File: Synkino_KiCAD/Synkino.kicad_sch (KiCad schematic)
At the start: 161 parts, among them J1 Pwr, J10 EYE8_OUT, J11 EYE4_OUT, J12 2.5mm, J13 EYE5_OUT, J2 2.5mm, J3 3.5mm, J4 Micro_SD_Card_Det_Hirose_DM3AT, J5 EYE1_OUT, J6 EYE6_OUT, J7 EYE2_OUT, J8 EYE7_OUT, J9 EYE3_OUT, Q1 IRF7319, Q2 BC847 o. SS8050, Q3 IRLML2244 o. AO3401A, SW1 SW_Push, SW2 Rotary_Encoder_Switch, SW3 SW_Push, U1 MCP1702T-5002E/MB, U10 ATMEGA328P-AU, U11 QRE1113, U12 QRE1113, U13 QRE1113, U14 QRE1113, U15 QRE1113, U16 QRE1113, U17 24LC256, U18 QRE1113, U2 ATMEGA328P-AU, U3 74HC4050, U4 SPIOLED128x64, U5 AP7312-1833W6-7, U6 74HC14, U7 VS1053B, U8 MAX4741, U9 QRE1113, X1 FTDIconn, X2 ICSP, X3 FTDIconn, X4 ICSP, Y1 16Mhz, Y2 12.288MHz, Y3 16Mhz

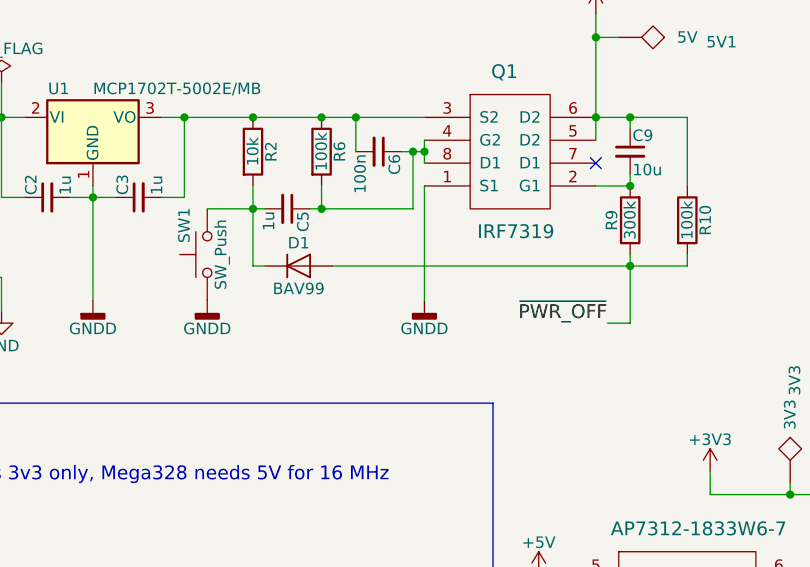
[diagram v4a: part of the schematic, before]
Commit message: Updating Reset Button, Footprints, adding 3v3 pane to Audio part
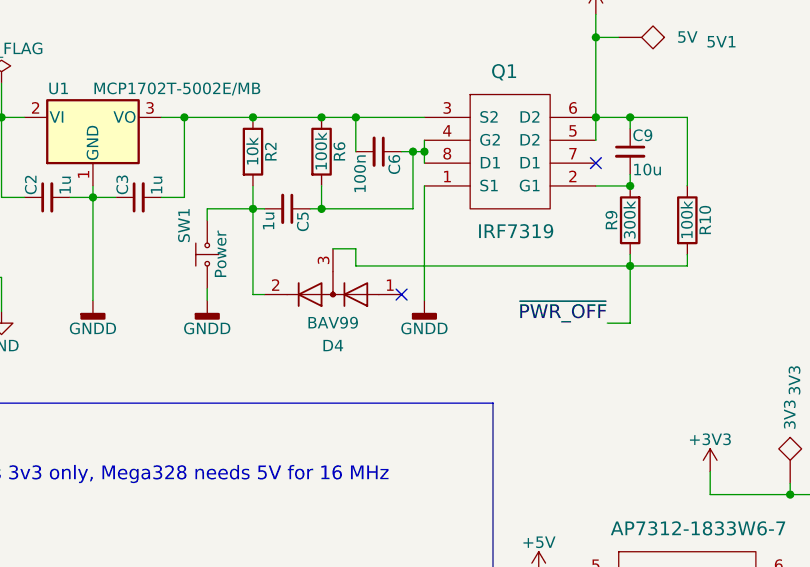
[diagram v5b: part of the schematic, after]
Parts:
- removed D1: BAV99, easyeda2kicad:SOT-23-3_L2.9-W1.3-P1.90-LS2.4-BR, symbol Synkino:D
- added D4: BAV99, Package_TO_SOT_SMD:SOT-23, symbol Diode:BAV99
- GND2, GNDA1: footprint TestPoint:TestPoint_Pad_2.0x2.0mm -> TestPoint:TestPoint_Pad_1.5x1.5mm
- J10, J11, J13, J5, J6, J7, J8, J9: footprint Connector_PinSocket_2.54mm:PinSocket_1x03_P2.54mm_Vertical -> Connector_PinHeader_2.54mm:PinHeader_1x03_P2.54mm_Vertical
- SW1: value SW_Push -> Power; symbol Synkino:SW_Push -> easyeda2kicad:B3F-5000_sm; LCSC Part (none) -> C93156
- X1, X3: footprint Connector_PinSocket_2.54mm:PinSocket_1x06_P2.54mm_Vertical -> Connector_PinHeader_2.54mm:PinHeader_1x06_P2.54mm_Vertical
- X2, X4: footprint Connector_PinSocket_2.54mm:PinSocket_2x03_P2.54mm_Vertical -> Connector_PinHeader_2.54mm:PinHeader_2x03_P2.54mm_Vertical
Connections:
- net GND: now also SW1.3, SW1.4; no longer SW1.1
- net ~{PWR_OFF}: now also D4.3 (K)
- net at C5.2, R2.2, SW1.2: now also SW1.1, D4.2 (A)
- no-connect marks 12 -> 13
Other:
- moved on the sheet: SW1
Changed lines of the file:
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@@
   (no_connect (at 242.57 54.61))
   (no_connect (at 292.1 132.08))
+  (no_connect (at 86.36 53.975))
   (no_connect (at 107.95 39.37))
   (no_connect (at 307.34 38.1))
@@
     (stroke (width 0) (type default))
   )
+  (wire (pts (xy 78.74 48.895) (xy 81.28 48.895))
+    (stroke (width 0) (type default))
+  )
   (wire (pts (xy 191.77 80.01) (xy 194.31 80.01))
     (stroke (width 0) (type default))
@@
     (stroke (width 0) (type default))
   )
+  (wire (pts (xy 69.85 53.975) (xy 71.12 53.975))
+    (stroke (width 0) (type default))
+  )
   (wire (pts (xy 245.11 92.71) (xy 252.73 92.71))
     (stroke (width 0) (type default))
@@
     (stroke (width 0) (type default))
   )
+  (wire (pts (xy 64.77 44.45) (xy 64.77 45.72))
+    (stroke (width 0) (type default))
+  )
   (wire (pts (xy 100.33 185.42) (xy 100.33 220.98))
     (stroke (width 0) (type default))
@@
     (stroke (width 0) (type default))
   )
-  (wire (pts (xy 69.85 44.45) (xy 69.85 50.8))
+  (wire (pts (xy 69.85 44.45) (xy 69.85 53.975))
     (stroke (width 0) (type default))
   )
@@
     (stroke (width 0) (type default))
   )
+  (wire (pts (xy 81.28 48.895) (xy 81.28 50.8))
+    (stroke (width 0) (type default))
+  )
   (wire (pts (xy 104.14 196.85) (xy 114.3 196.85))
     (stroke (width 0) (type default))
@@
     (stroke (width 0) (type default))
   )
-  (wire (pts (xy 78.74 50.8) (xy 111.76 50.8))
+  (wire (pts (xy 81.28 50.8) (xy 111.76 50.8))
     (stroke (width 0) (type default))
   )
@@
     (stroke (width 0) (type default))
   )
-  (wire (pts (xy 69.85 50.8) (xy 71.12 50.8))
-    (stroke (width 0) (type default))
-  )
   (wire (pts (xy 372.11 68.58) (xy 372.11 62.23))
     (stroke (width 0) (type default))
@@
     (stroke (width 0) (type default))
   )
+  (wire (pts (xy 64.77 53.34) (xy 64.77 54.61))
+    (stroke (width 0) (type default))
+  )
   (wire (pts (xy 170.18 111.76) (xy 170.18 114.3))
     (stroke (width 0) (type default))
@@
       (effects (font (size 1.524 1.524)))
     )
-    (property "Footprint" "Connector_PinSocket_2.54mm:PinSocket_2x03_P2.54mm_Vertical" (at 383.54 97.79 0)
+    (property "Footprint" "Connector_PinHeader_2.54mm:PinHeader_2x03_P2.54mm_Vertical" (at 383.54 97.79 0)
       (effects (font (size 1.524 1.524)) hide)
     )
@@
       (effects (font (size 1.524 1.524)))
     )
-    (property "Footprint" "Connector_PinSocket_2.54mm:PinSocket_1x06_P2.54mm_Vertical" (at 382.27 151.13 0)
+    (property "Footprint" "Connector_PinHeader_2.54mm:PinHeader_1x06_P2.54mm_Vertical" (at 382.27 151.13 0)
       (effects (font (size 1.524 1.524)) hide)
     )
@@
       (effects (font (size 1.524 1.524)))
     )
-    (property "Footprint" "Connector_PinSocket_2.54mm:PinSocket_2x03_P2.54mm_Vertical" (at 106.68 151.13 0)
+    (property "Footprint" "Connector_PinHeader_2.54mm:PinHeader_2x03_P2.54mm_Vertical" (at 106.68 151.13 0)
       (effects (font (size 1.524 1.524)) hide)
     )
@@
       (effects (font (size 1.524 1.524)))
     )
-    (property "Footprint" "Connector_PinSocket_2.54mm:PinSocket_1x06_P2.54mm_Vertical" (at 40.64 151.13 0)
+    (property "Footprint" "Connector_PinHeader_2.54mm:PinHeader_1x06_P2.54mm_Vertical" (at 40.64 151.13 0)
       (effects (font (size 1.524 1.524)) hide)
     )
@@
     )
   )
-  (symbol (lib_id "Synkino:D") (at 74.93 50.8 0) (unit 1)
-    (in_bom yes) (on_board yes) (dnp no)
-    (property "Reference" "D1" (at 74.93 48.26 0)
-      (effects (font (size 1.27 1.27)))
-    )
-    (property "Value" "BAV99" (at 74.93 53.34 0)
-      (effects (font (size 1.27 1.27)))
-    )
-    (property "Footprint" "easyeda2kicad:SOT-23-3_L2.9-W1.3-P1.90-LS2.4-BR" (at 74.93 50.8 0)
-      (effects (font (size 1.27 1.27)) hide)
-    )
-    (property "Datasheet" "" (at 74.93 50.8 0)
-      (effects (font (size 1.27 1.27)) hide)
-    )
-    (property "Inventory" "B" (at 74.93 50.8 0)
-      (effects (font (size 1.27 1.27)) hide)
-    )
-    (property "LCSC" "C2500" (at 74.93 50.8 0)
-      (effects (font (size 1.27 1.27)) hide)
-    )
-    (pin "1")
-    (pin "2")
-    (instances
-      (project "Synkino"
-        (path "/9d4924d9-a2ad-42f2-a951-8d7a9cc74761"
-          (reference "D1") (unit 1)
-        )
-      )
-    )
-  )
   (symbol (lib_id "Synkino:C_Small") (at 83.82 38.1 270) (unit 1)
     (in_bom yes) (on_board yes) (dnp no)
@@
     )
   )
-  (symbol (lib_id "Synkino:SW_Push") (at 64.77 49.53 90) (unit 1)
+  (symbol (lib_id "easyeda2kicad:B3F-5000_sm") (at 64.77 49.53 90) (unit 1)
     (in_bom yes) (on_board yes) (dnp no)
     (property "Reference" "SW1" (at 62.23 48.26 0)
       (effects (font (size 1.27 1.27)) (justify left))
     )
-    (property "Value" "SW_Push" (at 66.294 49.53 0)
+    (property "Value" "Power" (at 66.294 49.53 0)
       (effects (font (size 1.27 1.27)))
     )
-    (property "Footprint" "easyeda2kicad:KEY-TH_4P-L12.0-W12.0-P5.0-LS12.5-EH-small" (at 59.69 49.53 0)
+    (property "Footprint" "easyeda2kicad:KEY-TH_4P-L12.0-W12.0-P5.0-LS12.5-EH-small" (at 74.93 49.53 0)
       (effects (font (size 1.27 1.27)) hide)
     )
-    (property "Datasheet" "" (at 59.69 49.53 0)
+    (property "Datasheet" "https://lcsc.com/product-detail/Others_Omron-Electronics_B3F-5000_Omron-Electronics-B3F-5000_C93156.html" (at 77.47 49.53 0)
       (effects (font (size 1.27 1.27)) hide)
     )
@@
       (effects (font (size 1.27 1.27)) hide)
     )
+    (property "LCSC Part" "C93156" (at 80.01 49.53 0)
+      (effects (font (size 1.27 1.27)) hide)
+    )
     (pin "1")
     (pin "2")
+    (pin "4")
+    (pin "3")
     (instances
       (project "Synkino"
@@
       (effects (font (size 1.27 1.27)))
     )
-    (property "Footprint" "Connector_PinSocket_2.54mm:PinSocket_1x03_P2.54mm_Vertical" (at 339.09 181.61 0)
+    (property "Footprint" "Connector_PinHeader_2.54mm:PinHeader_1x03_P2.54mm_Vertical" (at 339.09 181.61 0)
       (effects (font (size 1.27 1.27)) hide)
     )
@@
       (effects (font (size 1.27 1.27)))
     )
-    (property "Footprint" "Connector_PinSocket_2.54mm:PinSocket_1x03_P2.54mm_Vertical" (at 309.88 181.61 0)
+    (property "Footprint" "Connector_PinHeader_2.54mm:PinHeader_1x03_P2.54mm_Vertical" (at 309.88 181.61 0)
       (effects (font (size 1.27 1.27)) hide)
     )
@@
       (effects (font (size 1.27 1.27)))
     )
-    (property "Footprint" "Connector_PinSocket_2.54mm:PinSocket_1x03_P2.54mm_Vertical" (at 400.05 181.61 0)
+    (property "Footprint" "Connector_PinHeader_2.54mm:PinHeader_1x03_P2.54mm_Vertical" (at 400.05 181.61 0)
       (effects (font (size 1.27 1.27)) hide)
     )
@@
       (effects (font (size 1.27 1.27)))
     )
-    (property "Footprint" "Connector_PinSocket_2.54mm:PinSocket_1x03_P2.54mm_Vertical" (at 370.84 181.61 0)
+    (property "Footprint" "Connector_PinHeader_2.54mm:PinHeader_1x03_P2.54mm_Vertical" (at 370.84 181.61 0)
       (effects (font (size 1.27 1.27)) hide)
     )
@@
       (effects (font (size 1.27 1.27)))
     )
-    (property "Footprint" "Connector_PinSocket_2.54mm:PinSocket_1x03_P2.54mm_Vertical" (at 309.88 220.98 0)
+    (property "Footprint" "Connector_PinHeader_2.54mm:PinHeader_1x03_P2.54mm_Vertical" (at 309.88 220.98 0)
       (effects (font (size 1.27 1.27)) hide)
     )
@@
       (effects (font (size 1.27 1.27)))
     )
-    (property "Footprint" "Connector_PinSocket_2.54mm:PinSocket_1x03_P2.54mm_Vertical" (at 370.84 220.98 0)
+    (property "Footprint" "Connector_PinHeader_2.54mm:PinHeader_1x03_P2.54mm_Vertical" (at 370.84 220.98 0)
       (effects (font (size 1.27 1.27)) hide)
     )
@@
       (effects (font (size 1.27 1.27)))
     )
-    (property "Footprint" "Connector_PinSocket_2.54mm:PinSocket_1x03_P2.54mm_Vertical" (at 339.09 220.98 0)
+    (property "Footprint" "Connector_PinHeader_2.54mm:PinHeader_1x03_P2.54mm_Vertical" (at 339.09 220.98 0)
       (effects (font (size 1.27 1.27)) hide)
     )
@@
       (effects (font (size 1.27 1.27)))
     )
-    (property "Footprint" "Connector_PinSocket_2.54mm:PinSocket_1x03_P2.54mm_Vertical" (at 400.05 220.98 0)
+    (property "Footprint" "Connector_PinHeader_2.54mm:PinHeader_1x03_P2.54mm_Vertical" (at 400.05 220.98 0)
       (effects (font (size 1.27 1.27)) hide)
     )
@@
       (effects (font (size 1.27 1.27)))
     )
-    (property "Footprint" "TestPoint:TestPoint_Pad_2.0x2.0mm" (at 209.55 121.92 0)
+    (property "Footprint" "TestPoint:TestPoint_Pad_1.5x1.5mm" (at 209.55 121.92 0)
       (effects (font (size 1.27 1.27)) hide)
     )
@@
       (effects (font (size 1.27 1.27)))
     )
-    (property "Footprint" "TestPoint:TestPoint_Pad_2.0x2.0mm" (at 204.47 121.92 0)
+    (property "Footprint" "TestPoint:TestPoint_Pad_1.5x1.5mm" (at 204.47 121.92 0)
       (effects (font (size 1.27 1.27)) hide)
     )
@@
         )
       )
+    )
+  )
+  (symbol (lib_id "Diode:BAV99") (at 78.74 53.975 180) (unit 1)
+    (in_bom yes) (on_board yes) (dnp no)
+    (property "Reference" "D4" (at 78.74 59.69 0)
+      (effects (font (size 1.27 1.27)))
+    )
+    (property "Value" "BAV99" (at 78.74 57.15 0)
+      (effects (font (size 1.27 1.27)))
+    )
+    (property "Footprint" "Package_TO_SOT_SMD:SOT-23" (at 78.74 41.275 0)
+      (effects (font (size 1.27 1.27)) hide)
+    )
+    (property "Datasheet" "https://assets.nexperia.com/documents/data-sheet/BAV99_SER.pdf" (at 78.74 53.975 0)
+      (effects (font (size 1.27 1.27)) hide)
+    )
+    (property "Inventory" "B" (at 78.74 53.975 0)
+      (effects (font (size 1.27 1.27)) hide)
+    )
+    (property "LCSC" "C2500" (at 78.74 53.975 0)
+      (effects (font (size 1.27 1.27)) hide)
+    )
+    (pin "2")
+    (pin "3")
+    (pin "1")
+    (instances
+      (project "Synkino"
+        (path "/9d4924d9-a2ad-42f2-a951-8d7a9cc74761"
+          (reference "D4") (unit 1)
+        )
+      )

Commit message: DRC mostly happy now
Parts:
- 3V3, 5V1: footprint TestPoint:TestPoint_Pad_1.5x1.5mm -> TestPoint:TestPoint_THTPad_1.5x1.5mm_Drill0.7mm
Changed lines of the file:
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@@
       (effects (font (size 1.27 1.27)))
     )
-    (property "Footprint" "TestPoint:TestPoint_Pad_1.5x1.5mm" (at 110.49 25.4 0)
+    (property "Footprint" "TestPoint:TestPoint_THTPad_1.5x1.5mm_Drill0.7mm" (at 110.49 25.4 0)
       (effects (font (size 1.27 1.27)) hide)
     )
@@
       (effects (font (size 1.27 1.27)))
     )
-    (property "Footprint" "TestPoint:TestPoint_Pad_1.5x1.5mm" (at 129.54 74.93 0)
+    (property "Footprint" "TestPoint:TestPoint_THTPad_1.5x1.5mm_Drill0.7mm" (at 129.54 74.93 0)
       (effects (font (size 1.27 1.27)) hide)
     )

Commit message: Updated legacy footprint associations
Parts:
- BZ1: footprint lib_fp:AAC801J-13 -> Peacemans_Footprints:AAC801J-13
- J12, J2: footprint Synkino:SJ1-2503 -> Peacemans_Footprints:SJ1-2503
- J3: footprint lib_fp:SJ1-352XNG -> Peacemans_Footprints:SJ1-352XNG
- J4: footprint lib_fp:HRS_DM3AT-SF-PEJM5 -> Peacemans_Footprints:HRS_DM3AT-SF-PEJM5
- SW2: footprint lib_fp:SW_PEC11 -> Peacemans_Footprints:SW_PEC11
- U11, U12, U13, U14, U15, U16, U18, U9: footprint lib_fp:QRE1113GR -> Peacemans_Footprints:QRE1113GR
- U4: footprint lib_fp:SPIOLED -> Peacemans_Footprints:SPIOLED
- U5: footprint lib_fp:AP7312 -> Peacemans_Footprints:AP7312
- Y1, Y2, Y3: footprint lib_fp:CRYSTAL_7A -> Peacemans_Footprints:CRYSTAL_7A
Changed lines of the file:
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@@
       (effects (font (size 1.524 1.524)))
     )
-    (property "Footprint" "lib_fp:AP7312" (at 114.3 88.9 0)
+    (property "Footprint" "Peacemans_Footprints:AP7312" (at 114.3 88.9 0)
       (effects (font (size 1.524 1.524)) hide)
     )
@@
       (effects (font (size 1.27 1.27)))
     )
-    (property "Footprint" "lib_fp:CRYSTAL_7A" (at 173.99 105.41 0)
+    (property "Footprint" "Peacemans_Footprints:CRYSTAL_7A" (at 173.99 105.41 0)
       (effects (font (size 1.27 1.27)) hide)
     )
@@
       (effects (font (size 1.27 1.27)) (justify right))
     )
-    (property "Footprint" "lib_fp:HRS_DM3AT-SF-PEJM5" (at 382.27 30.48 0)
+    (property "Footprint" "Peacemans_Footprints:HRS_DM3AT-SF-PEJM5" (at 382.27 30.48 0)
       (effects (font (size 1.27 1.27)) hide)
     )
@@
       (effects (font (size 1.524 1.524)))
     )
-    (property "Footprint" "lib_fp:SPIOLED" (at 118.11 276.86 0)
+    (property "Footprint" "Peacemans_Footprints:SPIOLED" (at 118.11 276.86 0)
       (effects (font (size 1.524 1.524)) hide)
     )
@@
       (effects (font (size 1.27 1.27)))
     )
-    (property "Footprint" "lib_fp:CRYSTAL_7A" (at 80.01 190.5 0)
+    (property "Footprint" "Peacemans_Footprints:CRYSTAL_7A" (at 80.01 190.5 0)
       (effects (font (size 1.27 1.27)) hide)
     )
@@
       (effects (font (size 1.27 1.27)))
     )
-    (property "Footprint" "lib_fp:SW_PEC11" (at 111.76 183.896 0)
+    (property "Footprint" "Peacemans_Footprints:SW_PEC11" (at 111.76 183.896 0)
       (effects (font (size 1.27 1.27)) hide)
     )
@@
       (effects (font (size 1.524 1.524)))
     )
-    (property "Footprint" "lib_fp:QRE1113GR" (at 321.31 205.74 90)
+    (property "Footprint" "Peacemans_Footprints:QRE1113GR" (at 321.31 205.74 90)
       (effects (font (size 1.524 1.524)) hide)
     )
@@
       (effects (font (size 1.27 1.27)))
     )
-    (property "Footprint" "lib_fp:CRYSTAL_7A" (at 347.98 115.57 0)
+    (property "Footprint" "Peacemans_Footprints:CRYSTAL_7A" (at 347.98 115.57 0)
       (effects (font (size 1.27 1.27)) hide)
     )
@@
       (effects (font (size 1.27 1.27)))
     )
-    (property "Footprint" "lib_fp:SJ1-352XNG" (at 256.54 171.45 0)
+    (property "Footprint" "Peacemans_Footprints:SJ1-352XNG" (at 256.54 171.45 0)
       (effects (font (size 1.27 1.27)) hide)
     )
@@
       (effects (font (size 1.524 1.524)))
     )
-    (property "Footprint" "lib_fp:QRE1113GR" (at 292.1 205.74 90)
+    (property "Footprint" "Peacemans_Footprints:QRE1113GR" (at 292.1 205.74 90)
       (effects (font (size 1.524 1.524)) hide)
     )
@@
       (effects (font (size 1.524 1.524)))
     )
-    (property "Footprint" "lib_fp:QRE1113GR" (at 382.27 205.74 90)
+    (property "Footprint" "Peacemans_Footprints:QRE1113GR" (at 382.27 205.74 90)
       (effects (font (size 1.524 1.524)) hide)
     )
@@
       (effects (font (size 1.524 1.524)))
     )
-    (property "Footprint" "lib_fp:QRE1113GR" (at 353.06 205.74 90)
+    (property "Footprint" "Peacemans_Footprints:QRE1113GR" (at 353.06 205.74 90)
       (effects (font (size 1.524 1.524)) hide)
     )
@@
       (effects (font (size 1.524 1.524)))
     )
-    (property "Footprint" "lib_fp:QRE1113GR" (at 292.1 245.11 90)
+    (property "Footprint" "Peacemans_Footprints:QRE1113GR" (at 292.1 245.11 90)
       (effects (font (size 1.524 1.524)) hide)
     )
@@
       (effects (font (size 1.524 1.524)))
     )
-    (property "Footprint" "lib_fp:QRE1113GR" (at 353.06 245.11 90)
+    (property "Footprint" "Peacemans_Footprints:QRE1113GR" (at 353.06 245.11 90)
       (effects (font (size 1.524 1.524)) hide)
     )
@@
       (effects (font (size 1.524 1.524)))
     )
-    (property "Footprint" "lib_fp:QRE1113GR" (at 321.31 245.11 90)
+    (property "Footprint" "Peacemans_Footprints:QRE1113GR" (at 321.31 245.11 90)
       (effects (font (size 1.524 1.524)) hide)
     )
@@
       (effects (font (size 1.524 1.524)))
     )
-    (property "Footprint" "lib_fp:QRE1113GR" (at 382.27 245.11 90)
+    (property "Footprint" "Peacemans_Footprints:QRE1113GR" (at 382.27 245.11 90)
       (effects (font (size 1.524 1.524)) hide)
     )
@@
       (effects (font (size 1.27 1.27)))
     )
-    (property "Footprint" "Synkino:SJ1-2503" (at 175.26 231.14 0)
+    (property "Footprint" "Peacemans_Footprints:SJ1-2503" (at 175.26 231.14 0)
       (effects (font (size 1.27 1.27)) hide)
     )
@@
       (effects (font (size 1.27 1.27)))
     )
-    (property "Footprint" "Synkino:SJ1-2503" (at 175.26 247.65 0)
+    (property "Footprint" "Peacemans_Footprints:SJ1-2503" (at 175.26 247.65 0)
       (effects (font (size 1.27 1.27)) hide)
     )
@@
       (effects (font (size 1.27 1.27)) (justify left))
     )
-    (property "Footprint" "lib_fp:AAC801J-13" (at 389.255 25.4 90)
+    (property "Footprint" "Peacemans_Footprints:AAC801J-13" (at 389.255 25.4 90)
       (effects (font (size 1.27 1.27)) hide)
     )

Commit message: Lotsof cleanup
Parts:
- J3: footprint Peacemans_Footprints:SJ1-352XNG -> Peacemans_Footprints:SJ1-352XNG-3pin
- J4: footprint Peacemans_Footprints:HRS_DM3AT-SF-PEJM5 -> easyeda2kicad:SD-SMD_DM3AT-SF-PEJM5
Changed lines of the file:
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@@
       (effects (font (size 1.27 1.27)) (justify right))
     )
-    (property "Footprint" "Peacemans_Footprints:HRS_DM3AT-SF-PEJM5" (at 382.27 30.48 0)
+    (property "Footprint" "easyeda2kicad:SD-SMD_DM3AT-SF-PEJM5" (at 382.27 30.48 0)
       (effects (font (size 1.27 1.27)) hide)
     )
@@
       (effects (font (size 1.27 1.27)))
     )
-    (property "Footprint" "Peacemans_Footprints:SJ1-352XNG" (at 256.54 171.45 0)
-      (effects (font (size 1.27 1.27)) hide)
-    )
+    (property "Footprint" "Peacemans_Footprints:SJ1-352XNG-3pin" (at 256.54 171.45 0)
+      (effects (font (size 1.27 1.27)) hide)
+    )
